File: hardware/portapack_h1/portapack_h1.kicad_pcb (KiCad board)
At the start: 4 copper layers, 120 x 75 mm, 111 parts, among them J1 HEADER_1X3, J2 MICROSD_DETSW, J3 ER-TFT024-3_FPC, J4 HEADER_1X2, P1 CONN_COAX, P2 TRRS_SW_JACK, P20 HACKRF_ONE_P20, P22 HACKRF_ONE_P22, P28 HACKRF_ONE_P28, SW1 CK_TSWB-3N-CB, U1 AK4951EN, U2 TCR2EF18,LM(CT, U3 5M40ZE64, U4 CAT4004[_AB], U5 NUF4220MN, U6 BQ24075RGT, U7 74HC1G04GW, U8 MAX-M8, X1 10.00000M

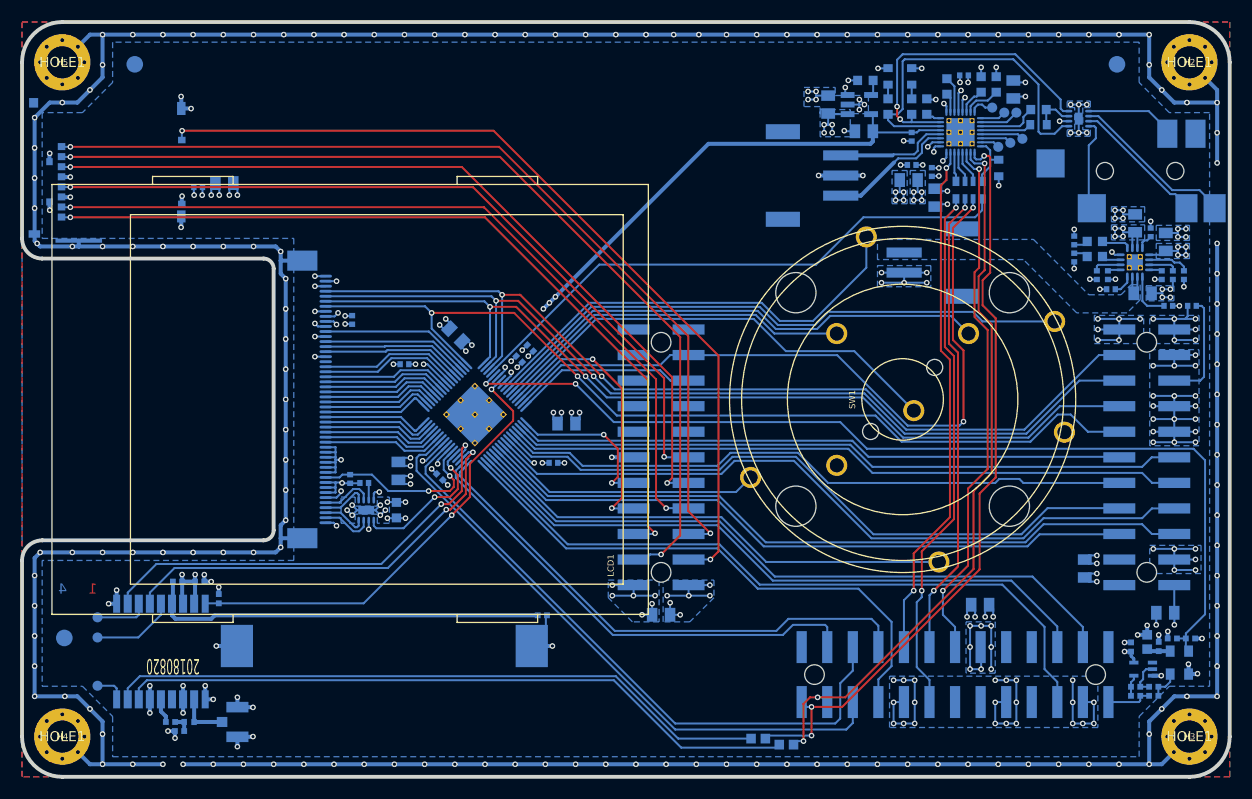
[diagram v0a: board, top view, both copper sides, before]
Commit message: Revert "Upstream merge to make new revision of PortaPack work (#206)"
This reverts commit 920b98f7c9a30371b643c42949066fb7d2441daf.

This pull request was missing some changes and was preventing firmware from functioning on older PortaPacks.
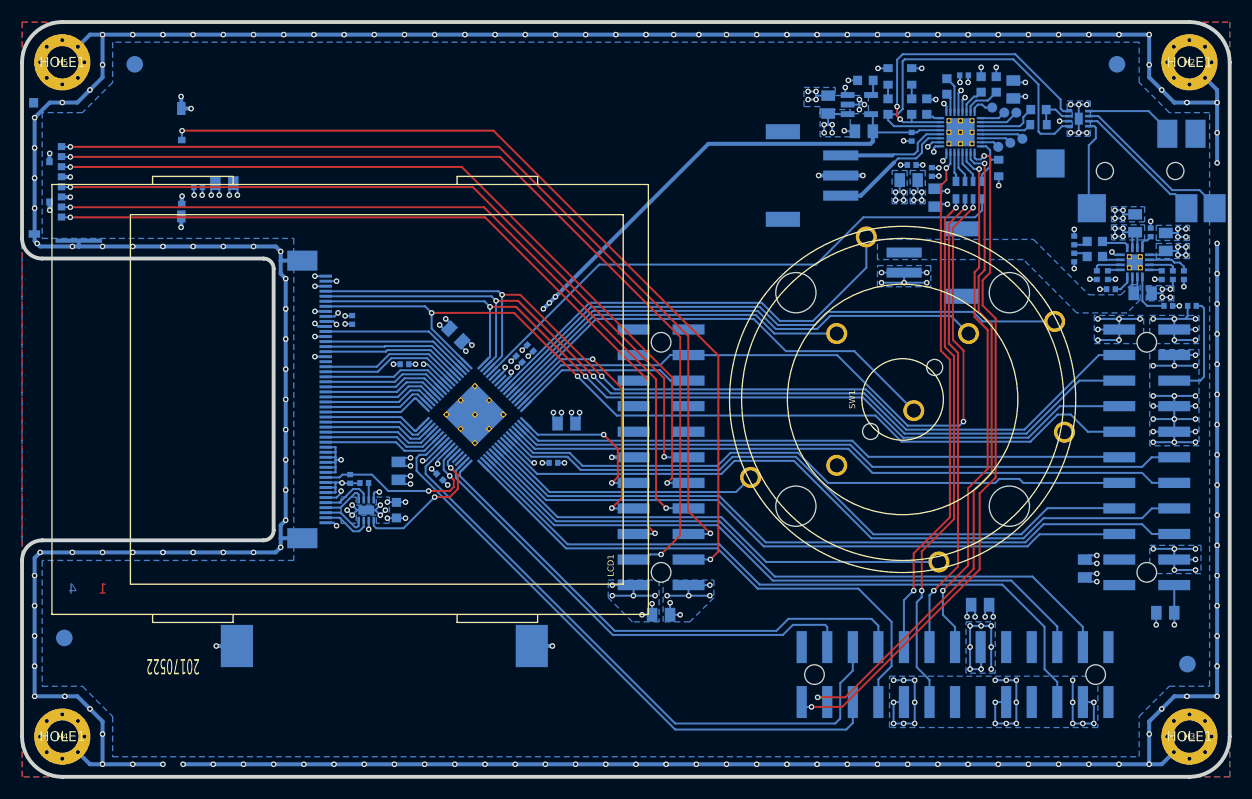
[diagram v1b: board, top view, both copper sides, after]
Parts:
- removed C17: 1N, ipc_capc:IPC_CAPC100X50X55L25N
- removed C18, C20, C9: 100N, ipc_capc:IPC_CAPC100X50X55L25N
- removed C19: 10N, ipc_capc:IPC_CAPC100X50X55L25N
- removed FB1, FB2, FB3: FBEAD, ipc_beadc:IPC_BEADC160X80X95L40N
- removed L1: 27N, ipc_indc:IPC_INDC100X50X60L20N
- removed P1: CONN_COAX, amp_te:1909763-1
- removed R15, R16: 10K, ipc_resc:IPC_RESC100X50X40L25N
- removed R17: 1M, ipc_resc:IPC_RESC100X50X40L25N
- removed R21, R22: 33R, ipc_resc:IPC_RESC100X50X40L25N
- removed R23, R24: 0R, ipc_resc:IPC_RESC100X50X40L25N
- removed R25: 100K, ipc_resc:IPC_RESC100X50X40L25N
- removed R26: 10R, ipc_resc:IPC_RESC100X50X40L25N
- removed TP7, TP8, TP9: TP, tp:TP_1MM
- removed U7: 74HC1G04GW, ipc_sot:IPC_SOT23-5P65_212X110L33X22N
- removed U8: MAX-M8, ublox:MAX-M8
- removed X1: 10.00000M, ipc_osccc:IPC_OSCCC320X250X110L75X100N
- added FID4: FIDUCIAL, fiducial:FIDUCIAL_65MIL, B.Cu at (175.8, 163.8)
- C1: value 1U -> DNP
- C15, C16: value 4U7 -> DNP
- C39, R1: value R -> DNP
- C41: value 10U -> DNP
- D1: value LED 0603 green -> DNP
- D2: value LED 0603 yellow -> DNP
- J4: value HEADER_1X2 -> DNP
- R10, R13, R14, R8, R9: value 10K -> DNP
- R19, R2: value 10K -> DNI
- R20: value 3K9 -> DNI
- R3, R5: value 1K5 -> DNP
- R4: value 1K91 -> DNP
- R6: value 1K8 -> DNP
- R7: value 0R -> DNP
- U2: value TCR2EF18,LM(CT -> REGULATOR_SOT23_5
- U6: value BQ24075RGT -> DNP
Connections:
- net +1V8 renamed +1.8V
- net +3V3 renamed +3.3V
- J3 pad 33: (no net) -> Net-(J3-Pad33)
- P2 pad 5: (no net) -> Net-(P2-Pad5)
- P2 pad 6: (no net) -> Net-(P2-Pad6)
- P20 pad 2: (no net) -> Net-(P20-Pad2)
- P20 pad 4: (no net) -> Net-(P20-Pad4)
- P22 pad 1: (no net) -> Net-(P22-Pad1)
- P22 pad 12: (no net) -> Net-(P22-Pad12)
- P22 pad 14: (no net) -> Net-(P22-Pad14)
- P22 pad 25: (no net) -> Net-(P22-Pad25)
- P22 pad 7: (no net) -> Net-(P22-Pad7)
- P22 pad 8: (no net) -> Net-(P22-Pad8)
- P22 pad 9: (no net) -> Net-(P22-Pad9)
- P28 pad 13: (no net) -> Net-(P28-Pad13)
- P28 pad 14: (no net) -> Net-(P28-Pad14)
- P28 pad 15: (no net) -> Net-(P28-Pad15)
- P28 pad 16: (no net) -> Net-(P28-Pad16)
- P28 pad 18: (no net) -> Net-(P28-Pad18)
- P28 pad 20: (no net) -> Net-(P28-Pad20)
- P28 pad 21: (no net) -> Net-(P28-Pad21)
- P28 pad 22: (no net) -> Net-(P28-Pad22)
- U3 pad 35: /hackrf_if/GPS_TIMEPULSE -> Net-(U3-Pad35)
- U3 pad 36: /hackrf_if/GPS_TX_READY -> Net-(U3-Pad36)
- U3 pad 5: /hackrf_if/REF_EN -> Net-(U3-Pad5)
- U3 pad 7: /hackrf_if/GPS_RESET# -> Net-(U3-Pad7)
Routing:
- net /hackrf_if/REF_EN: track 96.6 -> 0.00 mm, vias 2 -> 0
- net Net-(FB1-Pad2): track 68.0 -> 0.00 mm
- net Net-(FB3-Pad2): track 66.1 -> 0.00 mm
- net /hackrf_if/GPS_RESET#: track 45.3 -> 0.00 mm, vias 2 -> 0
- net /hackrf_if/GPS_TX_READY: track 44.7 -> 0.00 mm, vias 2 -> 0
- net /hackrf_if/GPS_TIMEPULSE: track 42.5 -> 0.00 mm, vias 2 -> 0
- net Net-(R23-Pad1): track 40.0 -> 0.00 mm
- net GND: track 703.5 -> 680.4 mm, vias 314 -> 291
- net +3.3V: track 83.6 -> 72.0 mm, vias 56 -> 50
- net Net-(TP8-Pad1): track 8.33 -> 0.00 mm
- net /audio/SCL: track 75.9 -> 68.4 mm, vias 3 -> 2
- net /audio/SDA: track 72.5 -> 66.0 mm, vias 3 -> 2
- net Net-(TP9-Pad1): track 5.30 -> 0.00 mm
- net Net-(L1-Pad1): track 5.04 -> 0.00 mm
- net /hackrf_if/CLKIN: track 4.58 -> 0.00 mm
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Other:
- net class Default: clearance 0.159 -> 0.16
- rule pad_to_mask_clearance: 0.0508 -> 0.0762
- rule solder_mask_min_width: 0.1016 -> 0.0762
- rule trace_clearance: 0.159 -> 0.16
- board text added: "20170522"
- board text removed: "20180820"
